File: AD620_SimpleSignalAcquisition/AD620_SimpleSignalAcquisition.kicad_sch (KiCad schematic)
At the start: 15 parts, among them J1 signal, U1 ATmega328P-A, U2 AD620, U3 ICL7660

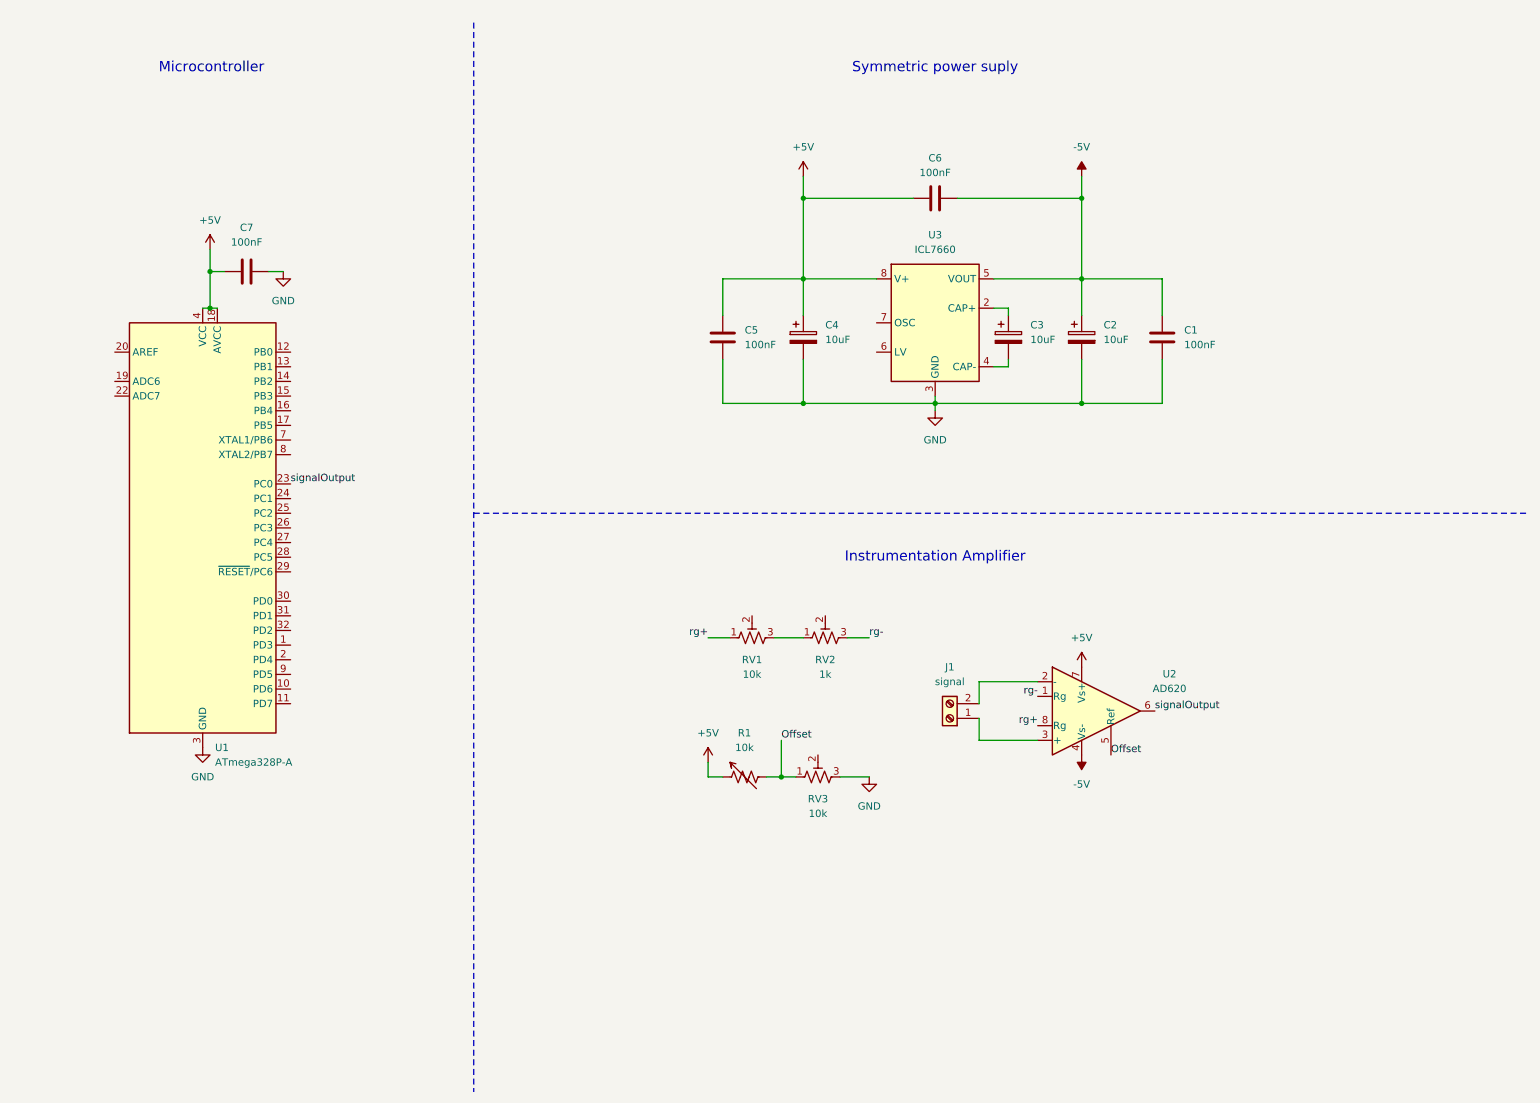
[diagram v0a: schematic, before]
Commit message: LCD Display
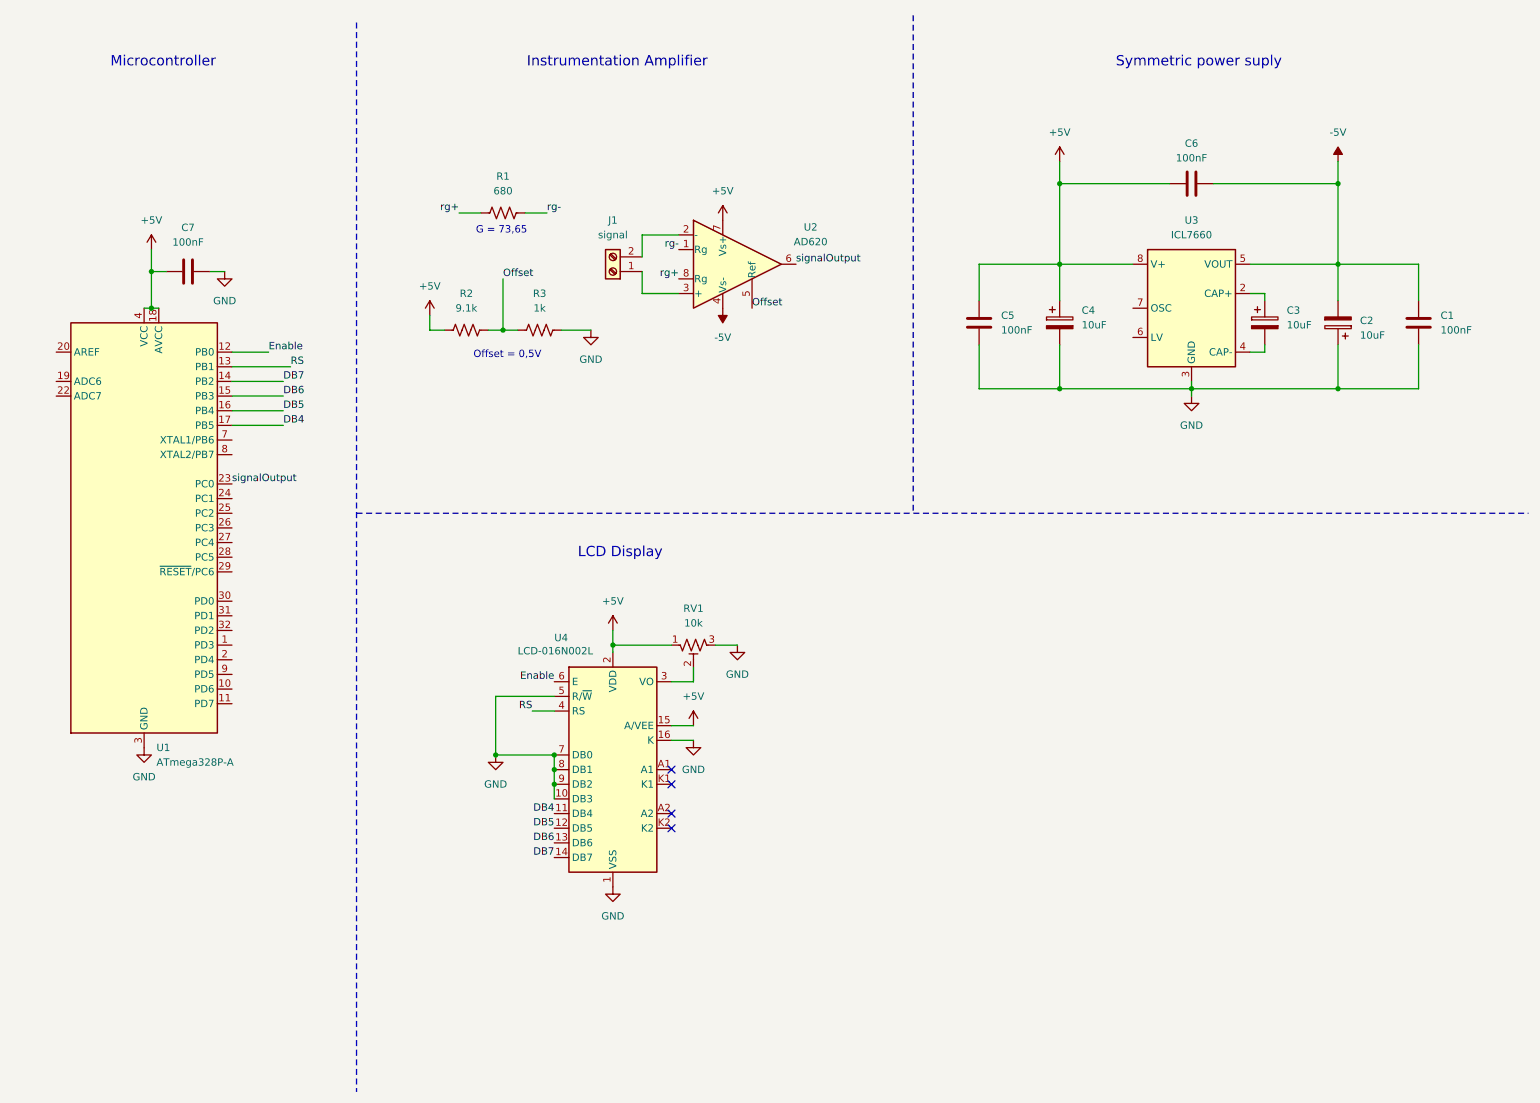
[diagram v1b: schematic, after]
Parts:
- removed R1: 10k, symbol Device:R_Variable_US
- removed RV2: 1k, symbol Device:R_Potentiometer_Trim_US
- removed RV3: 10k, symbol Device:R_Potentiometer_Trim_US
- added R1: 680, symbol Device:R_US
- added R2: 9.1k, symbol Device:R_US
- added R3: 1k, symbol Device:R_US
- added U4: LCD-016N002L, Display:LCD-016N002L, symbol Display_Character:LCD-016N002L
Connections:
- net +5V: now also RV1.1, R2.1, U4.15 (A/VEE), U4.2 (VDD)
- net -5V: now also C2.2; no longer C2.1
- net GND: now also C2.1, RV1.3, R3.2, U4.1 (VSS), U4.10 (DB3), U4.16 (K), U4.5 (R/~{W}), U4.7 (DB0), U4.8 (DB1), U4.9 (DB2); no longer C2.2
- net Offset: now also R2.2, R3.1
- net rg+: now also R1.1; no longer RV1.1
- net rg-: now also R1.2
- net Enable: now reaches U1.12 (PB0)
- net Enable: now also U4.6 (E)
- net RS: now reaches U1.13 (PB1)
- net RS: now also U4.4 (RS)
- net DB7: now reaches U1.14 (PB2)
- net DB7: now also U4.14 (DB7)
- net DB6: now reaches U1.15 (PB3)
- net DB6: now also U4.13 (DB6)
- net DB5: now reaches U1.16 (PB4)
- net DB5: now also U4.12 (DB5)
- net DB4: now reaches U1.17 (PB5)
- net DB4: now also U4.11 (DB4)
- net at RV1.2: now also U4.3 (VO)
- no-connect marks 0 -> 4
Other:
- note added: "G = 73,65"
- note added: "LCD Display"
- note added: "Offset = 0,5V"
- moved on the sheet: C1, C2, C3, C4, C5, C6, C7, J1, U1, U2, U3

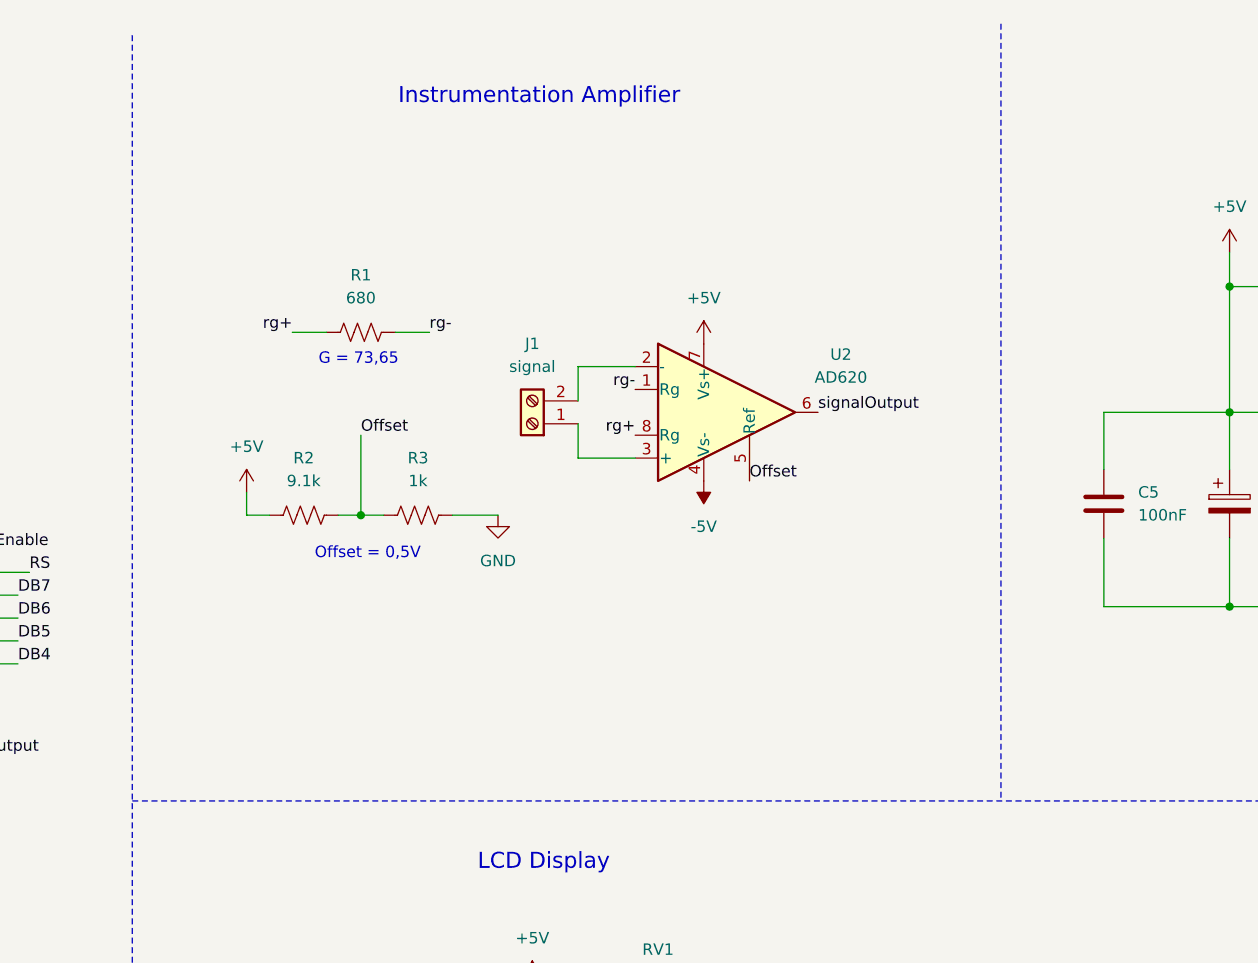
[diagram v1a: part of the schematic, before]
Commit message: Implementacao de firmware de leitura
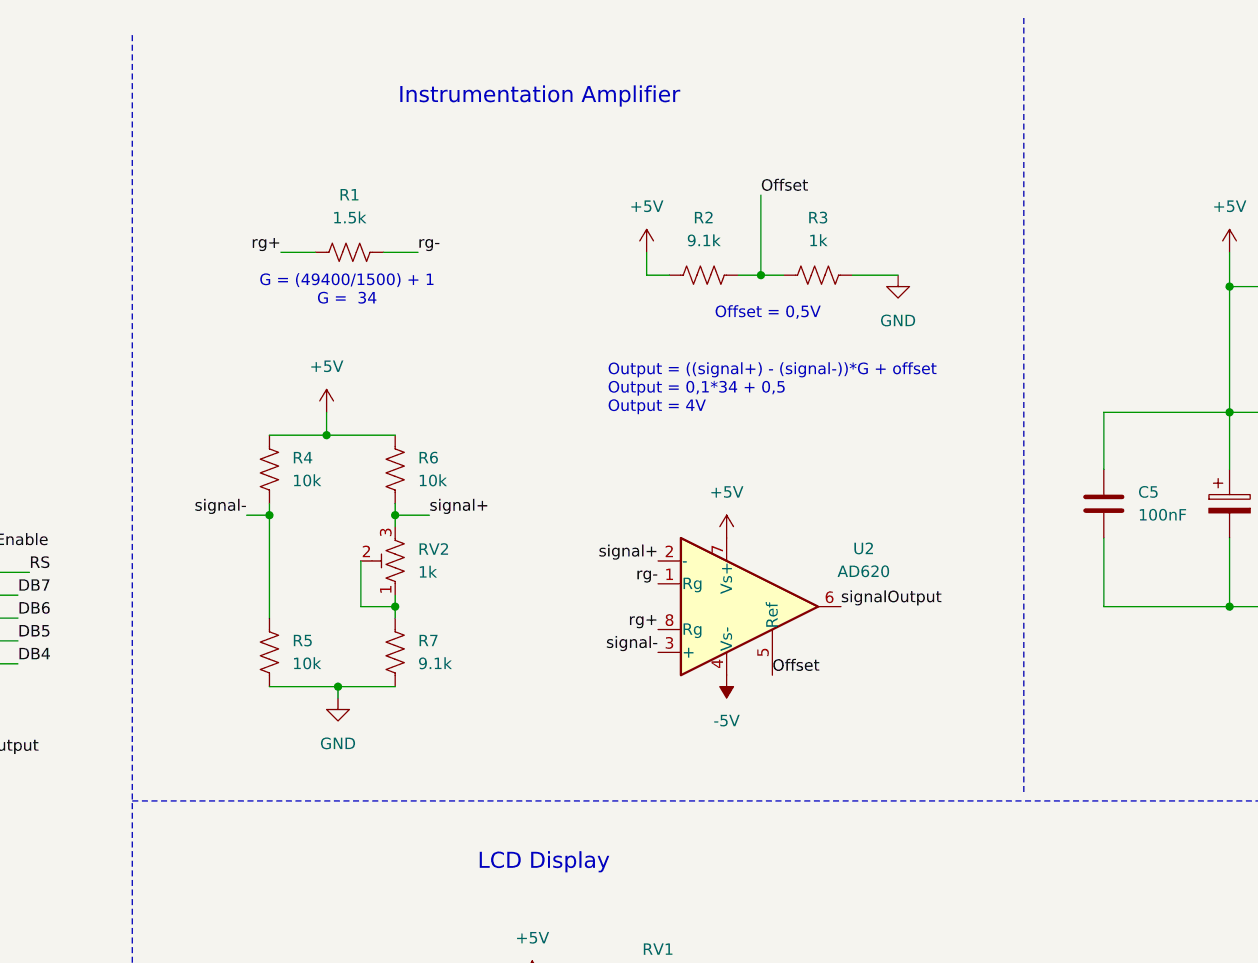
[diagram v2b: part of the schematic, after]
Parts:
- removed J1: signal, symbol Connector:Screw_Terminal_01x02
- added R4, R5, R6: 10k, symbol Device:R_US
- added R7: 9.1k, symbol Device:R_US
- added RV2: 1k, symbol Device:R_Potentiometer_Trim_US
- R1: value 680 -> 1.5k
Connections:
- net +5V: now also R4.1, R6.1
- net GND: now also R5.2, R7.2
- net signal-: now reaches U2.3 (+)
- net signal-: now also R4.2, R5.1
- net signal+: now reaches U2.2 (-)
- net signal+: now also R6.2, RV2.3
- new net: R7.1, RV2.1, RV2.2
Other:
- note added: "G = (49400/1500) + 1 G = 34"
- note added: "Output = ((signal+) - (signal-))*G + offset Output = 0,1*34 + 0,5 Output = 4V"
- note removed: "G = 73,65"
- moved on the sheet: R1, R2, R3, U2

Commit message: Serial communication
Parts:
- removed C7: 100nF, symbol Device:C
- removed R1: 1.5k, symbol Device:R_US
- removed R2, R7: 9.1k, symbol Device:R_US
- removed R3: 1k, symbol Device:R_US
- removed R4, R5, R6: 10k, symbol Device:R_US
- removed RV1: 10k, symbol Device:R_Potentiometer_Trim_US
- removed RV2: 1k, symbol Device:R_Potentiometer_Trim_US
- removed U1: ATmega328P-A, Package_QFP:TQFP-32_7x7mm_P0.8mm, symbol MCU_Microchip_ATmega:ATmega328P-A
- removed U2: AD620, symbol Amplifier_Instrumentation:AD620
- removed U4: LCD-016N002L, Display:LCD-016N002L, symbol Display_Character:LCD-016N002L
- added A1: Arduino_UNO_R3, Module:Arduino_UNO_R3, symbol MCU_Module:Arduino_UNO_R3
- added J1: USB_A, symbol Connector:USB_A
- added R10: 1.5k, symbol Device:R_US
- added R11, R8, R9: 10k, symbol Device:R_US
- added R12, R13: 9.1k, symbol Device:R_US
- added R14: 1k, symbol Device:R_US
- added RV3: 1k, symbol Device:R_Potentiometer_Trim_US
- added U1: CH340C, Package_SO:SOIC-16_3.9x9.9mm_P1.27mm, symbol Interface_USB:CH340C
- added U4: AD620, symbol Amplifier_Instrumentation:AD620
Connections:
- net +5V: now also R11.1, R13.1, R8.1, U4.7 (Vs+)
- net -5V: now also U4.4 (Vs-)
- net GND: now also R12.2, R14.2, R9.2
- net Offset: now also R13.2, R14.1, U4.5 (Ref)
- net rg+: now also R10.1, U4.8 (Rg)
- net rg-: now also R10.2, U4.1 (Rg)
- net signal+: now also R11.2, RV3.3, U4.2 (-)
- net signal-: now also R8.2, R9.1, U4.3 (+)
- net signalOutput: now also A1.9 (A0), U4.6
- new net: R12.1, RV3.1, RV3.2
- new net: J1.3 (D+), U1.5 (UD+)
- new net: J1.2 (D-), U1.6 (UD-)
- new net +5V USB: A1.8 (VIN), J1.1 (VBUS), U1.16 (VCC)
- new net GND USB: A1.29 (GND), A1.6 (GND), A1.7 (GND), J1.4 (GND), U1.1 (GND)
- new net RXD: A1.15 (D0/RX), U1.2 (TXD)
- new net TXD: A1.16 (D1/TX), U1.3 (RXD)
- no-connect marks 4 -> 3
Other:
- note added: "External power supply"
- note added: "Output = ((signal+) - (signal-))*G + offset Output = 0,1*34 + 0,5 Output = 3,9V"
- note removed: "LCD Display"
- note removed: "Output = ((signal+) - (signal-))*G + offset Output = 0,1*34 + 0,5 Output = 4V"
- moved on the sheet: C1, C2, C3, C4, C5, C6, U3

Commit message: Updating schematic
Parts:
- R13: value 9.1k -> 91
- R14: value 1k -> 10
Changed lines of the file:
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@@
 			)
 		)
-		(property "Value" "1k"
+		(property "Value" "10"
 			(at 252.73 144.78 90)
 			(show_name no)
@@
 			)
 		)
-		(property "Value" "9.1k"
+		(property "Value" "91"
 			(at 240.03 144.78 90)
 			(show_name no)
